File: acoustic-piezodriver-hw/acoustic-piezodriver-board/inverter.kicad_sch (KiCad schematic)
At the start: 35 parts, among them J1 Conn_02x04_Odd_Even, U2 UCC27282DR, U3 UCC27282DR, U6 NCE6005AS, U7 NCE6005AS

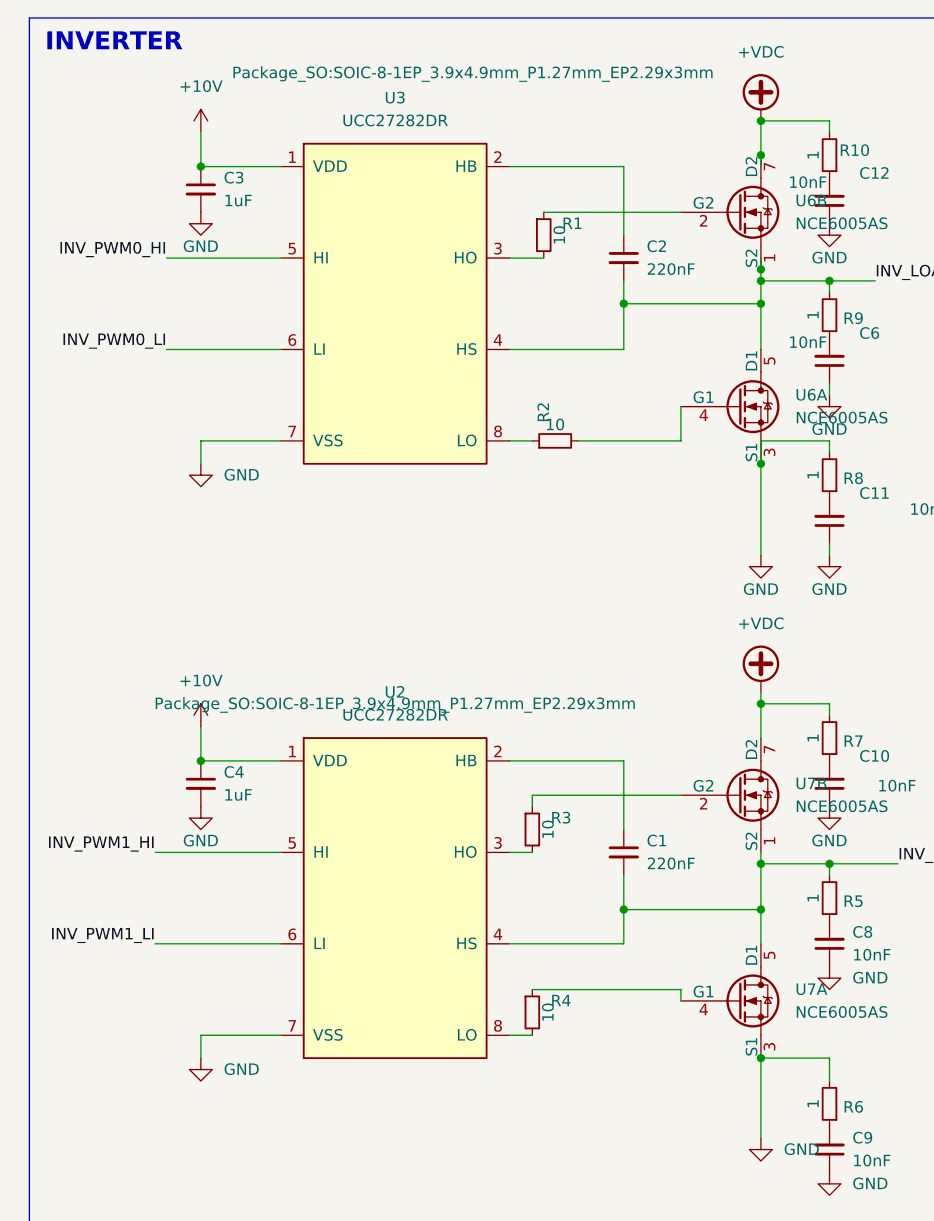
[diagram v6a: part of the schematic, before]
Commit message: [carrier] Added second adc input with magnetics, added ethernet connector with magnetics [piezodriver] Added diodes to level shifters for gate charge return current
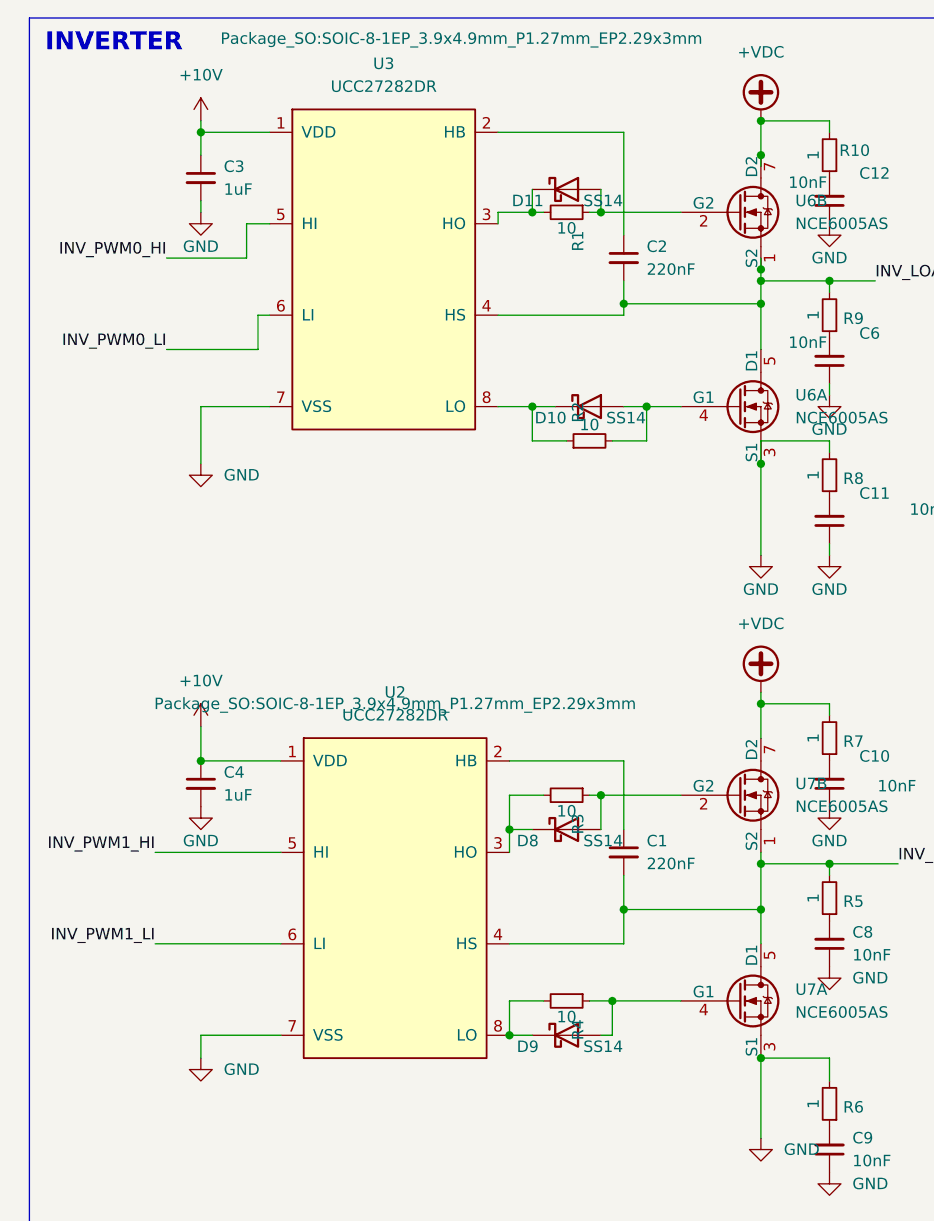
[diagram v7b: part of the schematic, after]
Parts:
- added D10, D11, D8, D9: SS14, Diode_SMD:D_SMA, symbol Diode:SS14
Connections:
- net at R4.1, U7.4 (G1): now also D9.2 (A)
- net at R4.2, U2.8 (LO): now also D9.1 (K)
- net at R2.1, U3.8 (LO): now also D10.1 (K)
- net at R2.2, U6.4 (G1): now also D10.2 (A)
- net at R1.1, U6.2 (G2): now also D11.2 (A)
- net at R3.2, U2.3 (HO): now also D8.1 (K)
- net at R3.1, U7.2 (G2): now also D8.2 (A)
- net at R1.2, U3.3 (HO): now also D11.1 (K)
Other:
- moved on the sheet: C3, R1, R2, R3, R4, U3

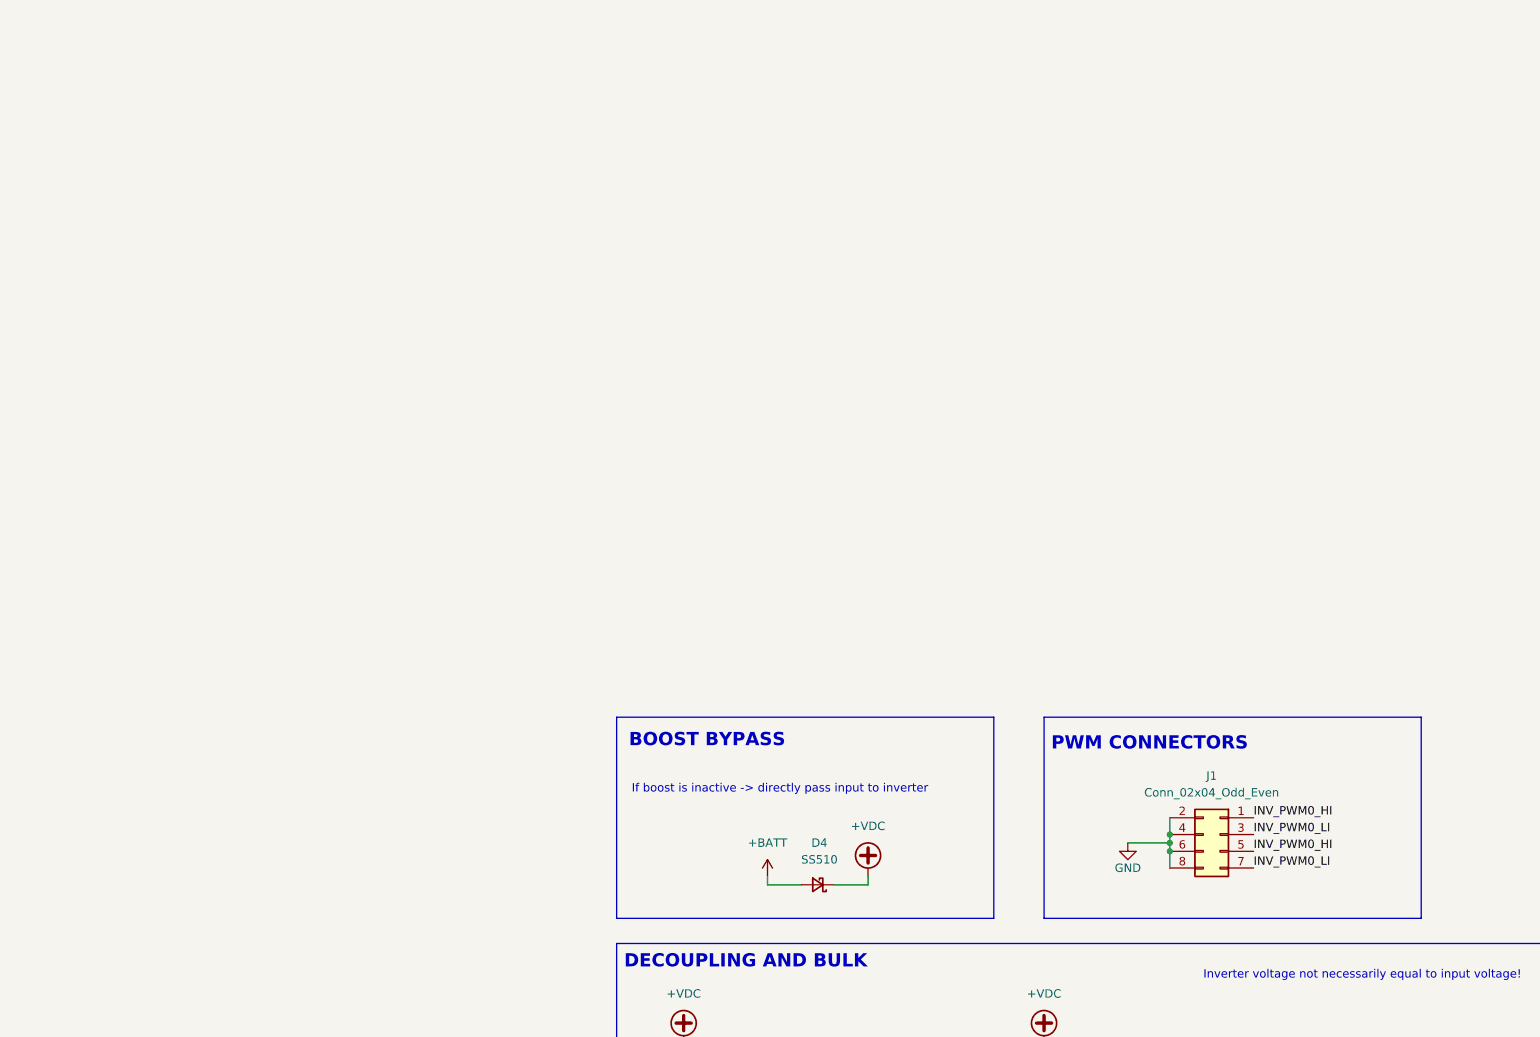
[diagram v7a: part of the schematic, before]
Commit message: [piezodriver] Added temperature sensors + ldo + 8x2 connectors to carrier board
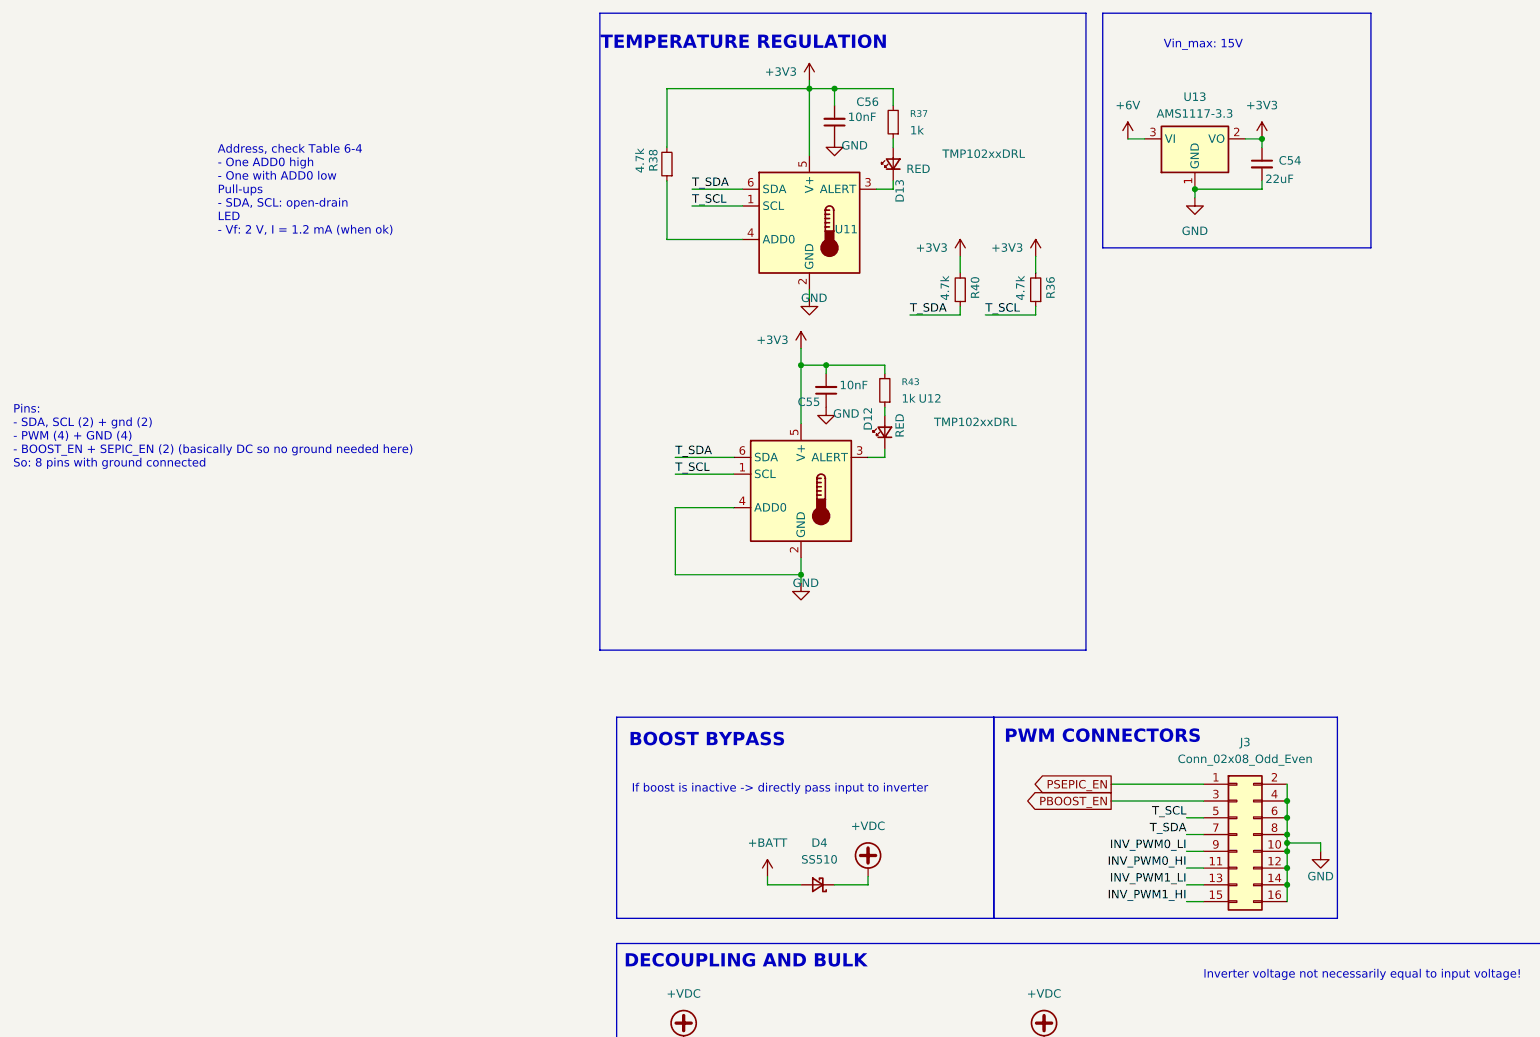
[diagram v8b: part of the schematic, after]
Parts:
- removed J1: Conn_02x04_Odd_Even, Connector_PinHeader_2.54mm:PinHeader_2x04_P2.54mm_Horizontal, symbol Connector_Generic:Conn_02x04_Odd_Even
- added C54: 22uF, Capacitor_SMD:C_0805_2012Metric, symbol Device:C_Small
- added C55, C56: 10nF, Capacitor_SMD:C_0402_1005Metric, symbol Device:C_Small
- added D12, D13: RED, Diode_SMD:D_0603_1608Metric, symbol Device:LED_Small
- added J3: Conn_02x08_Odd_Even, Connector_PinHeader_2.54mm:PinHeader_2x08_P2.54mm_Horizontal, symbol Connector_Generic:Conn_02x08_Odd_Even
- added R36, R38, R40: 4.7k, Resistor_SMD:R_0402_1005Metric, symbol Device:R_Small
- added R37, R43: 1k, Resistor_SMD:R_0402_1005Metric, symbol Device:R_Small
- added U11, U12: TMP102xxDRL, Package_TO_SOT_SMD:SOT-563, symbol Sensor_Temperature:TMP102xxDRL
- added U13: AMS1117-3.3, Package_TO_SOT_SMD:SOT-223-3_TabPin2, symbol Regulator_Linear:AMS1117-3.3
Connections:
- net GND: now also C54.2, C55.1, C56.1, J3.10 (Pin_10), J3.12 (Pin_12), J3.14 (Pin_14), J3.16 (Pin_16), J3.2 (Pin_2), J3.4 (Pin_4), J3.6 (Pin_6), J3.8 (Pin_8), U11.2 (GND), U12.2 (GND), U12.4 (ADD0), U13.1 (GND)
- net INV_PWM0_HI: now also J3.11 (Pin_11)
- net INV_PWM0_LI: now also J3.9 (Pin_9)
- net INV_PWM1_HI: now also J3.15 (Pin_15)
- net INV_PWM1_LI: now also J3.13 (Pin_13)
- new net: D12.1 (K), U12.3 (ALERT)
- new net: R38.1, U11.4 (ADD0)
- new net: D13.1 (K), U11.3 (ALERT)
- new net: D13.2 (A), R37.1
- new net: D12.2 (A), R43.1
- new net +3V3: C54.1, C55.2, C56.2, R36.2, R37.2, R38.2, R40.2, R43.2, U11.5 (V+), U12.5 (V+), U13.2 (VO)
- new net +6V: U13.3 (VI)
- new net PBOOST_EN: J3.3 (Pin_3)
- new net PSEPIC_EN: J3.1 (Pin_1)
- new net T_SCL: J3.5 (Pin_5), R36.1, U11.1 (SCL), U12.1 (SCL)
- new net T_SDA: J3.7 (Pin_7), R40.1, U11.6 (SDA), U12.6 (SDA)
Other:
- note added: "Address, check Table 6-4 - One ADD0 high - One with ADD0 low Pull-ups - SDA, SCL: open-drain LED - Vf: 2 V, I = 1.2 mA (when ok)"
- note added: "Pins: - SDA, SCL (2) + gnd (2) - PWM (4) + GND (4) - BOOST_EN + SEPIC_EN (2) (basically DC so no ground needed here) So: 8 pins with ground connected"
- note added: "TEMPERATURE REGULATION"
- note added: "Vin_max: 15V"
